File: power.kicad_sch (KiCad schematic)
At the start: 22 parts, among them U3 LM66200DRLR, U4 MAX77827AEFD+T, U5 SC4215ASTRT

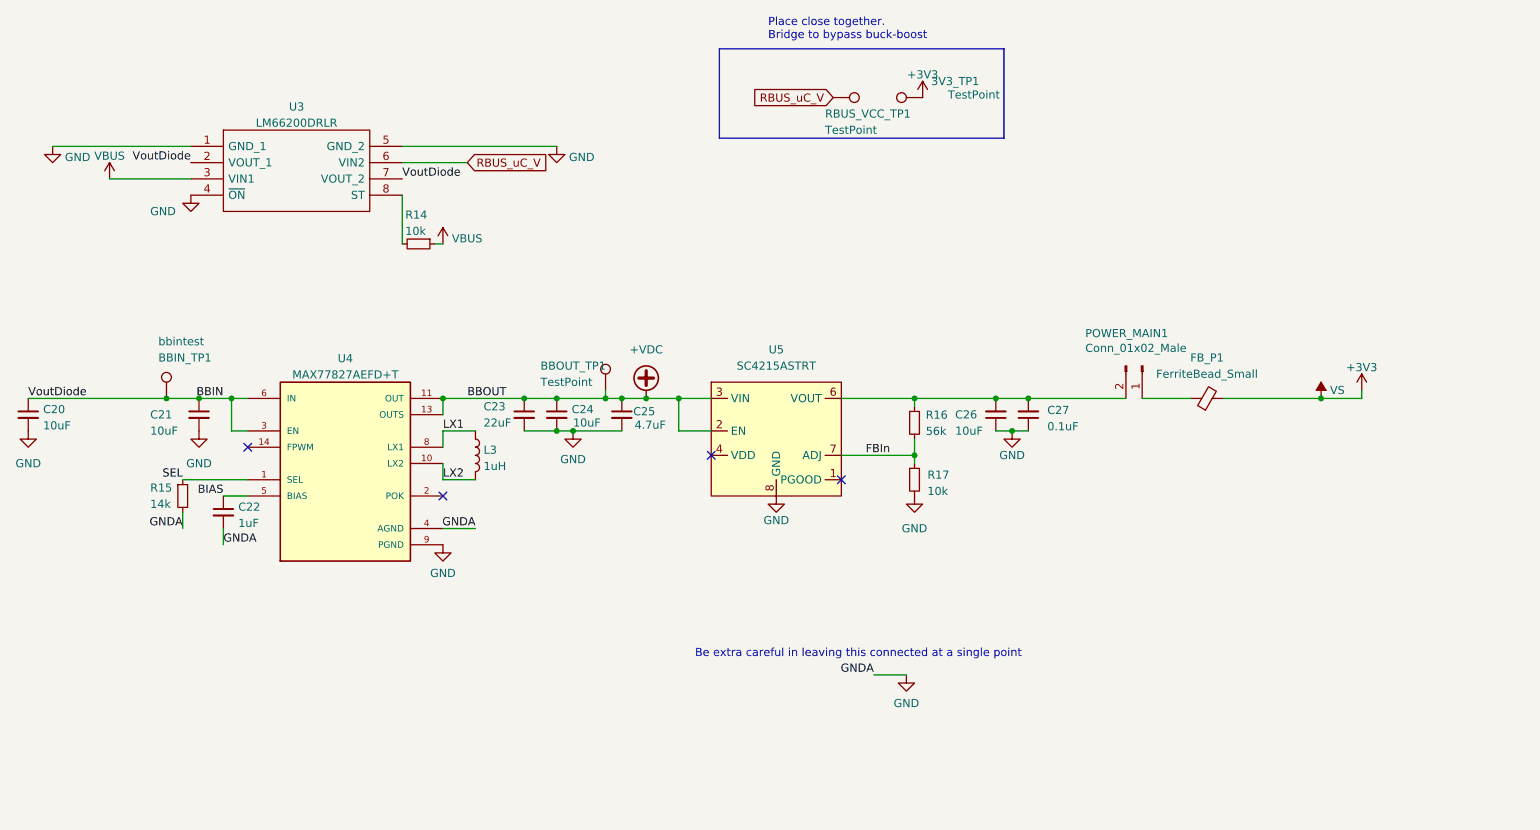
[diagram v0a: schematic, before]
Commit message: Fixed Libraries
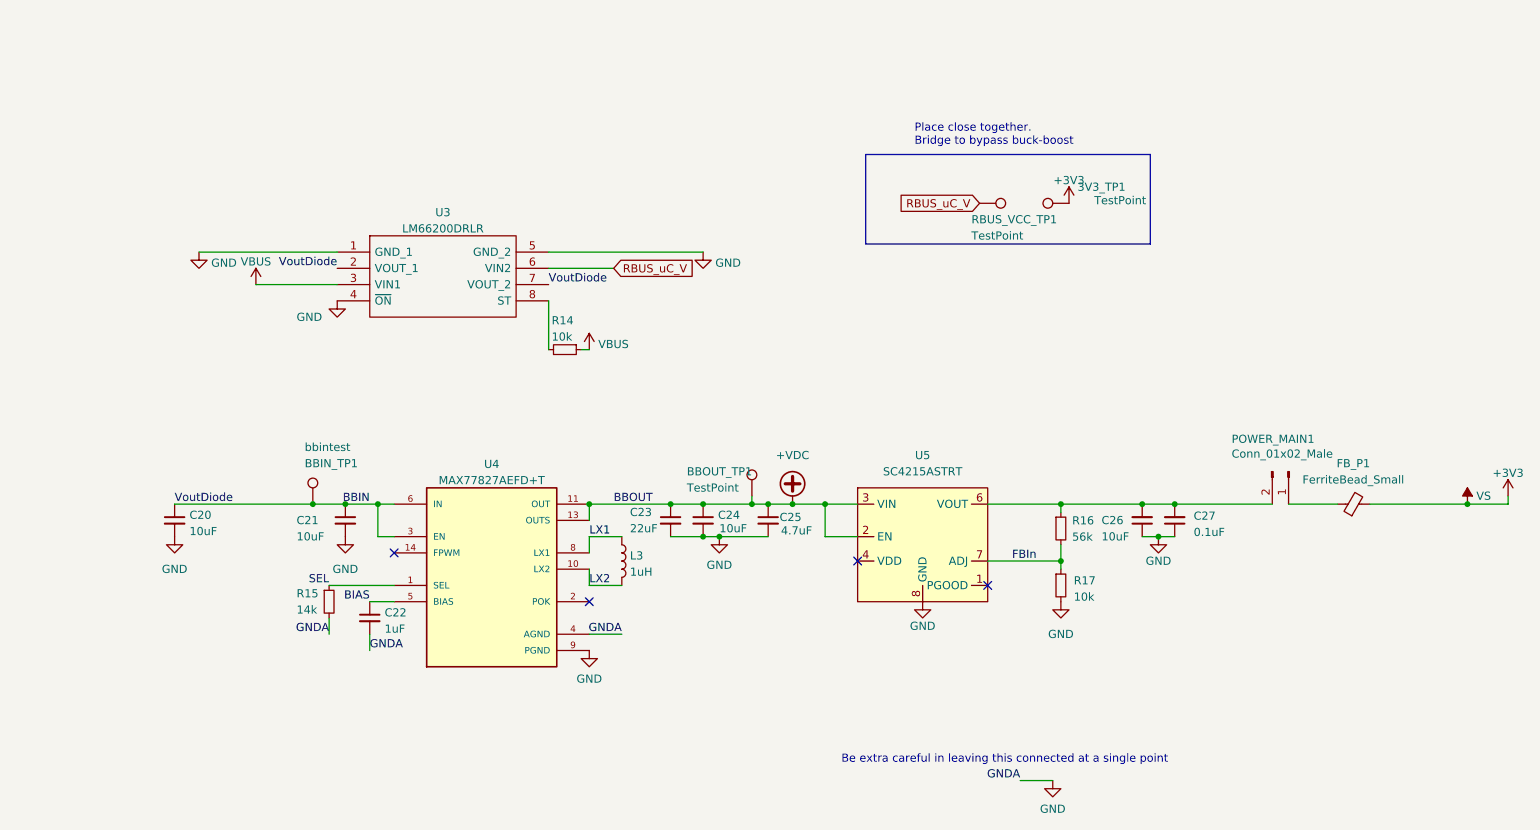
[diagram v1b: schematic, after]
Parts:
- U3: footprint footprints:SOTFL50P160X60-8N -> iclr:SOTFL50P160X60-8N
- U4: footprint footprints:CONV_MAX77827AEFD+T -> iclr:CONV_MAX77827AEFD+T
- U5: footprint footprints:SOIC127P599X175-9N -> iclr:SOIC127P599X175-9N
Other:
- moved on the sheet: 3V3_TP1, BBIN_TP1, BBOUT_TP1, C20, C21, C22, C23, C24, C25, C26, C27, FB_P1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

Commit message: Post review changes WIP
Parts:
- removed POWER_MAIN1: Conn_01x02_Male, Connector_PinHeader_2.54mm:PinHeader_1x02_P2.54mm_Vertical, symbol Connector:Conn_01x02_Male
- added J4: Conn_01x03_Pin, Connector_PinHeader_2.54mm:PinHeader_1x03_P2.54mm_Vertical, symbol Connector:Conn_01x03_Pin
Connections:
- net at C26.2, C27.2, R16.1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: now also J4.2 (Pin_2), J4.3 (Pin_3)
- net at FB_P1.1: now also J4.1 (Pin_1)
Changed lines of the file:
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@@
+	)
+	(junction
+		(at 213.36 92.71)
+		(diameter 0)
+		(color 0 0 0 0)
 	)
 	(junction
@@
 	(wire
 		(pts
+			(xy 213.36 92.71) (xy 215.9 92.71)
+		)
+		(stroke
+			(width 0)
+			(type default)
+		)
+	)
+	(wire
+		(pts
 			(xy 252.73 92.71) (xy 252.73 91.44)
 		)
@@
 	(wire
 		(pts
-			(xy 200.66 92.71) (xy 215.9 92.71)
+			(xy 200.66 92.71) (xy 213.36 92.71)
 		)
 		(stroke
@@
 	)
 	(symbol
+		(lib_id "Connector:Conn_01x03_Pin")
+		(at 215.9 87.63 270)
+		(unit 1)
+		(exclude_from_sim no)
+		(in_bom yes)
+		(on_board yes)
+		(dnp no)
+		(property "Reference" "J4"
+			(at 215.9 82.55 90)
+			(effects
+				(font
+					(size 1.27 1.27)
+				)
+			)
+		)
+		(property "Value" "Conn_01x03_Pin"
+			(at 215.9 85.09 90)
+			(effects
+				(font
+					(size 1.27 1.27)
+				)
+			)
+		)
+		(property "Footprint" "Connector_PinHeader_2.54mm:PinHeader_1x03_P2.54mm_Vertical"
+			(at 215.9 87.63 0)
+			(effects
+				(font
+					(size 1.27 1.27)
+				)
+				(hide yes)
+			)
+		)
+		(property "Datasheet" "~"
+			(at 215.9 87.63 0)
+			(effects
+				(font
+					(size 1.27 1.27)
+				)
+				(hide yes)
+			)
+		)
+		(property "Description" "Generic connector, single row, 01x03, script generated"
+			(at 215.9 87.63 0)
+			(effects
+				(font
+					(size 1.27 1.27)
+				)
+				(hide yes)
+			)
+		)
+		(pin "3"
+		)
+		(pin "2"
+		)
+		(pin "1"
+		)
+		(instances
+			(project "Ricardo-Hermes"
+				(path "/7db990e4-92e1-4f99-b4d2-435bbec1ba83/48a413b4-b7c2-44ac-971c-583c31b73475"
+					(reference "J4")
+					(unit 1)
+				)
+			)
+		)
+	)
+	(symbol
 		(lib_id "power:GND")
 		(at 161.29 107.95 0)
@@
 					(unit 1)
 				)
-			)
-		)
-	)
-	(symbol
-		(lib_id "Connector:Conn_01x02_Male")
-		(at 218.44 87.63 270)
-		(unit 1)
-		(exclude_from_sim no)
-		(in_bom yes)
-		(on_board yes)
-		(dnp no)
-		(property "Reference" "POWER_MAIN1"
-			(at 209.55 82.55 90)
-			(effects
-				(font
-					(size 1.27 1.27)
-				)
-				(justify left)
-			)
-		)
-		(property "Value" "Conn_01x02_Male"
-			(at 209.55 84.8614 90)
-			(effects
-				(font
-					(size 1.27 1.27)
-				)
-				(justify left)
-			)
-		)
-		(property "Footprint" "Connector_PinHeader_2.54mm:PinHeader_1x02_P2.54mm_Vertical"
-			(at 218.44 87.63 0)
-			(effects
-				(font
-					(size 1.27 1.27)
-				)
-				(hide yes)
-			)
-		)
-		(property "Datasheet" "~"
-			(at 218.44 87.63 0)
-			(effects
-				(font
-					(size 1.27 1.27)
-				)
-				(hide yes)
-			)
-		)
-		(property "Description" ""
-			(at 218.44 87.63 0)
-			(effects
-				(font
-					(size 1.27 1.27)
-				)
-				(hide yes)
-			)
-		)
-		(pin "1"
-		)
-		(pin "2"
-		)
-		(instances
-			(project "RicardoTemplate"
-				(path "/7db990e4-92e1-4f99-b4d2-435bbec1ba83/48a413b4-b7c2-44ac-971c-583c31b73475"
-					(reference "POWER_MAIN1")
-					(unit 1)
-				)

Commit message: Went for a 3v3 plane
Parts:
- removed J4: Conn_01x03_Pin, Connector_PinHeader_2.54mm:PinHeader_1x03_P2.54mm_Vertical, symbol Connector:Conn_01x03_Pin
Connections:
- net at C26.2, C27.2, R16.1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: now also FB_P1.1
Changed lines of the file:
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@@
-	)
-	(junction
-		(at 213.36 92.71)
-		(diameter 0)
-		(color 0 0 0 0)
 	)
 	(junction
@@
 	(wire
 		(pts
-			(xy 218.44 92.71) (xy 226.06 92.71)
-		)
-		(stroke
-			(width 0)
-			(type default)
-		)
-	)
-	(wire
-		(pts
 			(xy 102.87 68.58) (xy 102.87 60.96)
 		)
@@
 	(wire
 		(pts
-			(xy 213.36 92.71) (xy 215.9 92.71)
-		)
-		(stroke
-			(width 0)
-			(type default)
-		)
-	)
-	(wire
-		(pts
 			(xy 252.73 92.71) (xy 252.73 91.44)
 		)
@@
 	(wire
 		(pts
-			(xy 200.66 92.71) (xy 213.36 92.71)
+			(xy 200.66 92.71) (xy 226.06 92.71)
 		)
 		(stroke
@@
 					(unit 1)
 				)
-			)
-		)
-	)
-	(symbol
-		(lib_id "Connector:Conn_01x03_Pin")
-		(at 215.9 87.63 270)
-		(unit 1)
-		(exclude_from_sim no)
-		(in_bom yes)
-		(on_board yes)
-		(dnp no)
-		(property "Reference" "J4"
-			(at 215.9 82.55 90)
-			(effects
-				(font
-					(size 1.27 1.27)
-				)
-			)
-		)
-		(property "Value" "Conn_01x03_Pin"
-			(at 215.9 85.09 90)
-			(effects
-				(font
-					(size 1.27 1.27)
-				)
-			)
-		)
-		(property "Footprint" "Connector_PinHeader_2.54mm:PinHeader_1x03_P2.54mm_Vertical"
-			(at 215.9 87.63 0)
-			(effects
-				(font
-					(size 1.27 1.27)
-				)
-				(hide yes)
-			)
-		)
-		(property "Datasheet" "~"
-			(at 215.9 87.63 0)
-			(effects
-				(font
-					(size 1.27 1.27)
-				)
-				(hide yes)
-			)
-		)
-		(property "Description" "Generic connector, single row, 01x03, script generated"
-			(at 215.9 87.63 0)
-			(effects
-				(font
-					(size 1.27 1.27)
-				)
-				(hide yes)
-			)
-		)
-		(pin "3"
-		)
-		(pin "2"
-		)
-		(pin "1"
-		)
-		(instances
-			(project "Ricardo-Hermes"
-				(path "/7db990e4-92e1-4f99-b4d2-435bbec1ba83/48a413b4-b7c2-44ac-971c-583c31b73475"
-					(reference "J4")
-					(unit 1)
-				)
